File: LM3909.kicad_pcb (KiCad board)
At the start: 2 copper layers, 21 x 14 mm, 19 parts, among them J1 Conn_01x04, J2 Conn_01x04, Q1 MMBT3904, Q2B1 MMBT3906, Q3 MMBT3904, Q4 MMBT3904

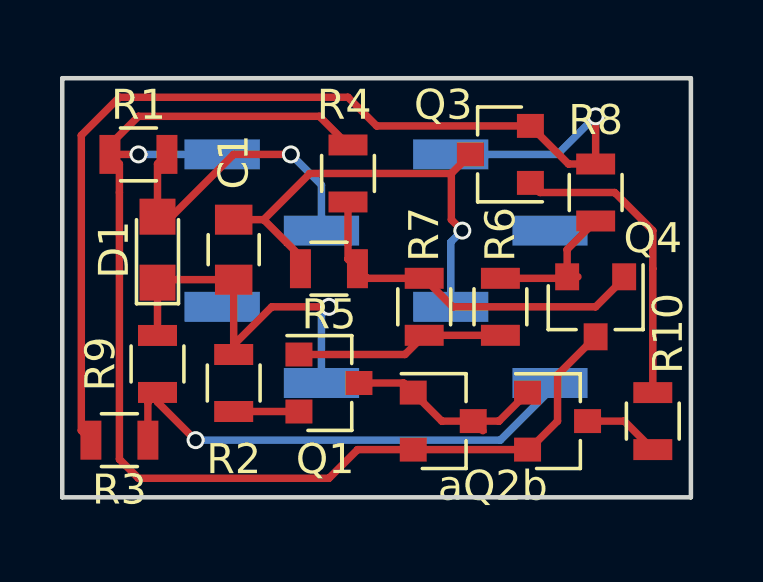
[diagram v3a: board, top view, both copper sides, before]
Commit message: move components and add pin 1 marker
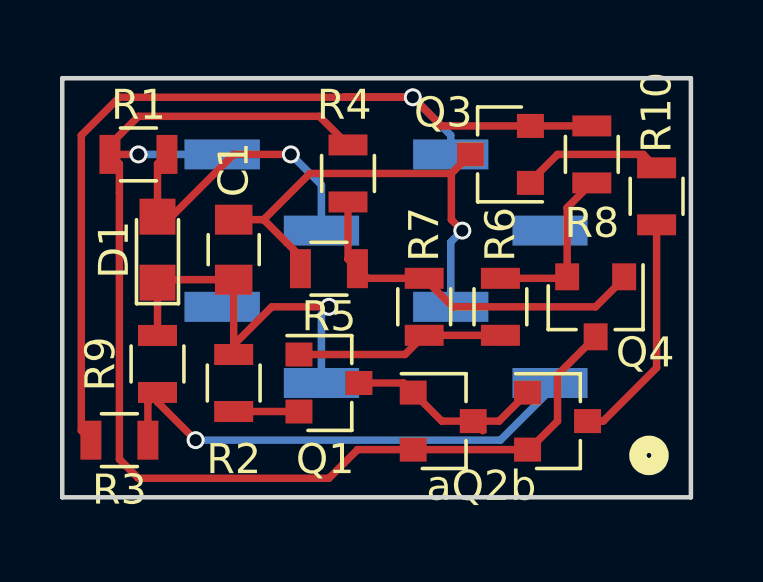
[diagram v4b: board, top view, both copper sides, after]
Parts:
- moved R10 7.49 mm to (139.8, 110.6)
- moved R8 1.28 mm to (137.7, 109.2)
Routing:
- net Net-(Q2B1-Pad3): track 2.57 -> 7.80 mm
- net Net-(Q3-Pad1): track 10.1 -> 5.13 mm
- net Net-(BT1-Pad2): track 35.8 -> 33.3 mm
- net Net-(Q4-Pad2): track 4.86 -> 5.89 mm
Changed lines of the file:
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@@
     (links 32)
     (no_connects 0)
-    (area 119.939999 105.695 142.575 123.045)
+    (area 119.939999 105.695 142.702 123.045)
     (thickness 1.6)
-    (drawings 4)
-    (tracks 104)
+    (drawings 5)
+    (tracks 105)
     (zones 0)
     (modules 19)
@@
   (layers
     (0 F.Cu signal)
-    (31 B.Cu signal hide)
+    (31 B.Cu signal)
     (32 B.Adhes user hide)
     (33 F.Adhes user hide)
@@
     (zone_45_only no)
     (trace_min 0.2)
-    (segment_width 0.2)
+    (segment_width 0.75)
     (edge_width 0.15)
     (via_size 0.6)
@@
     (tags "capacitor 0805")
     (attr smd)
-    (fp_text reference C1 (at -2.921 0 270) (layer F.SilkS)
+    (fp_text reference C1 (at -2.667 0 270) (layer F.SilkS)
       (effects (font (size 1 1) (thickness 0.15)))
     )
@@
     (tags "resistor 0805")
     (attr smd)
-    (fp_text reference R5 (at 0 -1.524 180) (layer F.SilkS)
+    (fp_text reference R5 (at 0 -1.5875 180) (layer F.SilkS)
       (effects (font (size 1 1) (thickness 0.15)))
     )
@@
   )
   (module Resistors_SMD:R_0805 (layer F.Cu)
-    (at 137.795 110.49 90)
+    (at 137.668 109.22 90)
     (descr "Resistor SMD 0805, reflow soldering, Vishay (see dcrcw.pdf)")
     (tags "resistor 0805")
     (attr smd)
-    (fp_text reference R8 (at 2.413 0 180) (layer F.SilkS)
+    (fp_text reference R8 (at -2.286 0 180) (layer F.SilkS)
       (effects (font (size 1 1) (thickness 0.15)))
     )
@@
     (tags SOT-23)
     (attr smd)
-    (fp_text reference aQ2b (at 1.651 2.159) (layer F.SilkS)
+    (fp_text reference aQ2b (at 1.27 2.159) (layer F.SilkS)
       (effects (font (size 1 1) (thickness 0.15)))
     )
@@
     (tags SOT-23)
     (attr smd)
-    (fp_text reference Q3 (at 1.905 1.651 180) (layer F.SilkS)
+    (fp_text reference Q3 (at 1.905 1.397 180) (layer F.SilkS)
       (effects (font (size 1 1) (thickness 0.15)))
     )
@@
     (tags SOT-23)
     (attr smd)
-    (fp_text reference Q4 (at -2.286 -1.905 360) (layer F.SilkS)
+    (fp_text reference Q4 (at 1.524 -1.651 360) (layer F.SilkS)
       (effects (font (size 1 1) (thickness 0.15)))
     )
@@
   )
   (module Resistors_SMD:R_0805 (layer F.Cu)
-    (at 139.7 118.11 90)
+    (at 139.827 110.617 90)
     (descr "Resistor SMD 0805, reflow soldering, Vishay (see dcrcw.pdf)")
     (tags "resistor 0805")
     (attr smd)
-    (fp_text reference R10 (at 2.921 0.508 90) (layer F.SilkS)
+    (fp_text reference R10 (at 2.794 0 90) (layer F.SilkS)
       (effects (font (size 1 1) (thickness 0.15)))
     )
@@
     )
   )
+  (gr_circle (center 139.573 119.253) (end 139.827 119.126) (layer F.SilkS) (width 0.75))
   (gr_line (start 120.015 120.65) (end 120.015 106.68) (angle 90) (layer Edge.Cuts) (width 0.15))
   (gr_line (start 140.97 120.65) (end 120.015 120.65) (angle 90) (layer Edge.Cuts) (width 0.15))
@@
   (segment (start 121.92 109.535) (end 121.605 109.22) (width 0.25) (layer F.Cu) (net 7))
   (segment (start 131.715 119.06) (end 131.715 119.11) (width 0.25) (layer F.Cu) (net 7))
-  (segment (start 137.525 118.11) (end 138.75 118.11) (width 0.25) (layer F.Cu) (net 8))
-  (segment (start 138.75 118.11) (end 139.7 119.06) (width 0.25) (layer F.Cu) (net 8))
-  (segment (start 132.965 109.22) (end 136.525 109.22) (width 0.25) (layer B.Cu) (net 9))
-  (segment (start 137.795 107.95) (end 137.795 109.54) (width 0.25) (layer F.Cu) (net 9))
-  (via (at 137.795 107.95) (size 0.6) (drill 0.4) (layers F.Cu B.Cu) (net 9))
-  (segment (start 136.525 109.22) (end 137.795 107.95) (width 0.25) (layer B.Cu) (net 9))
-  (segment (start 135.62 108.27) (end 130.495 108.27) (width 0.25) (layer F.Cu) (net 9))
+  (segment (start 137.525 118.11) (end 138.049 118.11) (width 0.25) (layer F.Cu) (net 8))
+  (segment (start 139.827 116.332) (end 139.827 111.567) (width 0.25) (layer F.Cu) (net 8))
+  (segment (start 138.049 118.11) (end 139.827 116.332) (width 0.25) (layer F.Cu) (net 8))
+  (segment (start 135.62 108.27) (end 137.668 108.27) (width 0.25) (layer F.Cu) (net 9))
+  (segment (start 129.413 107.315) (end 131.699 107.315) (width 0.25) (layer F.Cu) (net 9))
+  (segment (start 132.965 108.581) (end 132.965 109.22) (width 0.25) (layer B.Cu) (net 9))
+  (segment (start 131.699 107.315) (end 132.965 108.581) (width 0.25) (layer B.Cu) (net 9))
+  (via (at 131.699 107.315) (size 0.6) (drill 0.4) (layers F.Cu B.Cu) (net 9))
+  (segment (start 135.874 108.016) (end 135.62 108.27) (width 0.25) (layer F.Cu) (net 9))
+  (segment (start 135.62 108.27) (end 132.654 108.27) (width 0.25) (layer F.Cu) (net 9))
   (segment (start 120.65 108.585) (end 120.65 118.425) (width 0.25) (layer F.Cu) (net 9))
   (segment (start 121.92 107.315) (end 120.65 108.585) (width 0.25) (layer F.Cu) (net 9))
-  (segment (start 129.54 107.315) (end 121.92 107.315) (width 0.25) (layer F.Cu) (net 9))
-  (segment (start 130.495 108.27) (end 129.54 107.315) (width 0.25) (layer F.Cu) (net 9))
+  (segment (start 131.699 107.315) (end 129.413 107.315) (width 0.25) (layer F.Cu) (net 9))
+  (segment (start 129.413 107.315) (end 121.92 107.315) (width 0.25) (layer F.Cu) (net 9))
+  (segment (start 132.654 108.27) (end 131.699 107.315) (width 0.25) (layer F.Cu) (net 9))
   (segment (start 120.65 118.425) (end 120.97 118.745) (width 0.25) (layer F.Cu) (net 9))
-  (segment (start 137.795 109.54) (end 136.89 109.54) (width 0.25) (layer F.Cu) (net 9))
-  (segment (start 136.89 109.54) (end 135.62 108.27) (width 0.25) (layer F.Cu) (net 9))
-  (segment (start 136.845 113.3) (end 136.845 112.39) (width 0.25) (layer F.Cu) (net 10))
-  (segment (start 136.845 112.39) (end 137.795 111.44) (width 0.25) (layer F.Cu) (net 10))
-  (segment (start 136.845 113.3) (end 137.205 113.3) (width 0.25) (layer F.Cu) (net 10))
+  (segment (start 136.845 113.3) (end 136.845 110.993) (width 0.25) (layer F.Cu) (net 10))
+  (segment (start 136.845 110.993) (end 137.668 110.17) (width 0.25) (layer F.Cu) (net 10))
+  (segment (start 136.845 113.3) (end 137.017 113.3) (width 0.25) (layer F.Cu) (net 10))
   (segment (start 134.62 113.35) (end 136.795 113.35) (width 0.25) (layer F.Cu) (net 10))
   (segment (start 136.795 113.35) (end 136.845 113.3) (width 0.25) (layer F.Cu) (net 10))
@@
   (segment (start 132.08 113.35) (end 130.175 113.35) (width 0.25) (layer F.Cu) (net 11))
   (segment (start 130.175 113.35) (end 129.855 113.03) (width 0.25) (layer F.Cu) (net 11))
-  (segment (start 139.7 113.03) (end 139.7 111.76) (width 0.25) (layer F.Cu) (net 12))
-  (segment (start 138.43 110.49) (end 135.94 110.49) (width 0.25) (layer F.Cu) (net 12))
-  (segment (start 139.7 111.76) (end 138.43 110.49) (width 0.25) (layer F.Cu) (net 12))
-  (segment (start 135.94 110.49) (end 135.62 110.17) (width 0.25) (layer F.Cu) (net 12))
-  (segment (start 139.7 113.03) (end 139.7 117.16) (width 0.25) (layer F.Cu) (net 12))
-  (segment (start 139.7 113.03) (end 139.7 113.03) (width 0.25) (layer F.Cu) (net 12))
+  (segment (start 135.62 110.17) (end 135.62 110.125) (width 0.25) (layer F.Cu) (net 12))
+  (segment (start 135.62 110.125) (end 136.525 109.22) (width 0.25) (layer F.Cu) (net 12))
+  (segment (start 136.525 109.22) (end 139.38 109.22) (width 0.25) (layer F.Cu) (net 12))
+  (segment (start 139.38 109.22) (end 139.827 109.667) (width 0.25) (layer F.Cu) (net 12))
+  (segment (start 139.827 109.667) (end 139.512 109.667) (width 0.25) (layer F.Cu) (net 12))
   (segment (start 123.19 117.155) (end 123.19 117.475) (width 0.25) (layer F.Cu) (net 13))
   (segment (start 123.19 117.475) (end 124.46 118.745) (width 0.25) (layer F.Cu) (net 13))
